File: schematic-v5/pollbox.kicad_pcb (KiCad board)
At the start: 2 copper layers, 50.8 x 74.9 mm, 24 parts, among them P1 CONN_01X15, P10 CONN_01X04, P2 CONN_02X03, P20 CONN_01X04, P3 CONN_01X15, P30 CONN_01X04, P40 CONN_01X04, P50 CONN_01X04, U1 NodeMCU_1.0, U2 ULN2803

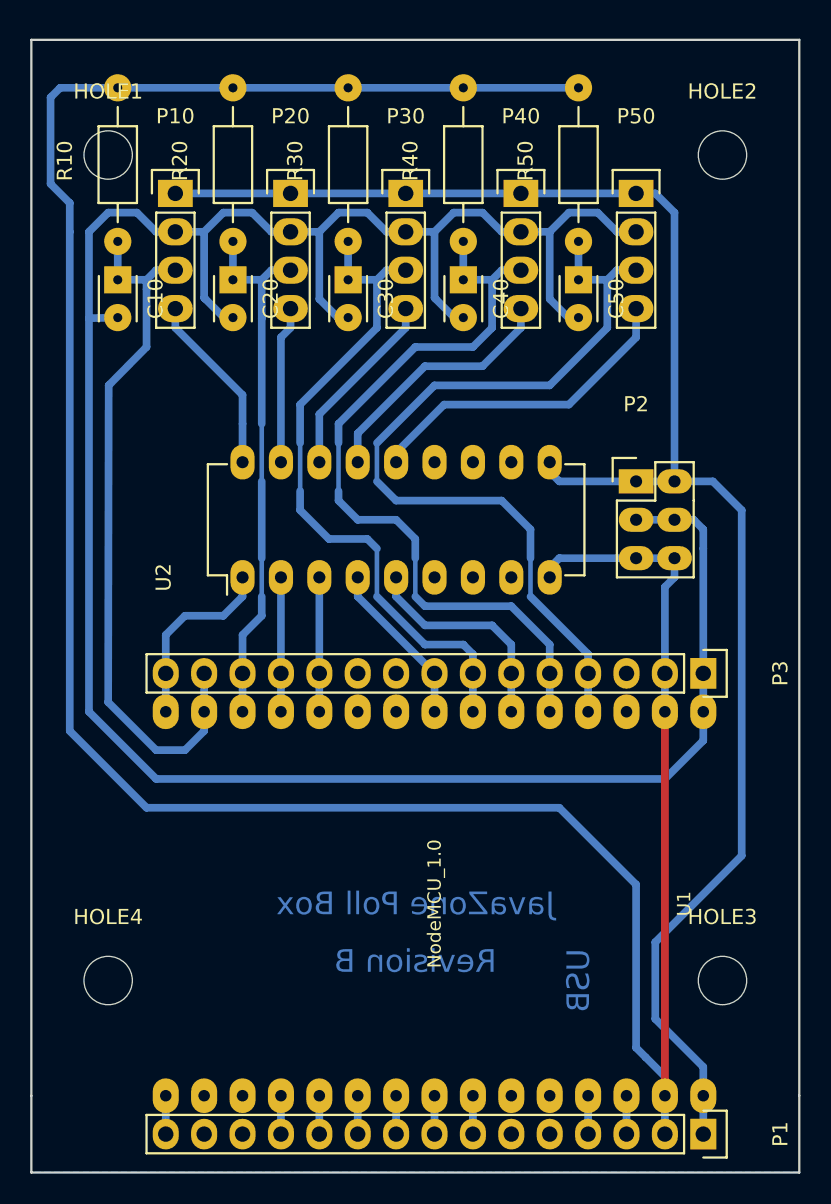
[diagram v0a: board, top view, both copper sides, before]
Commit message: reduce islands
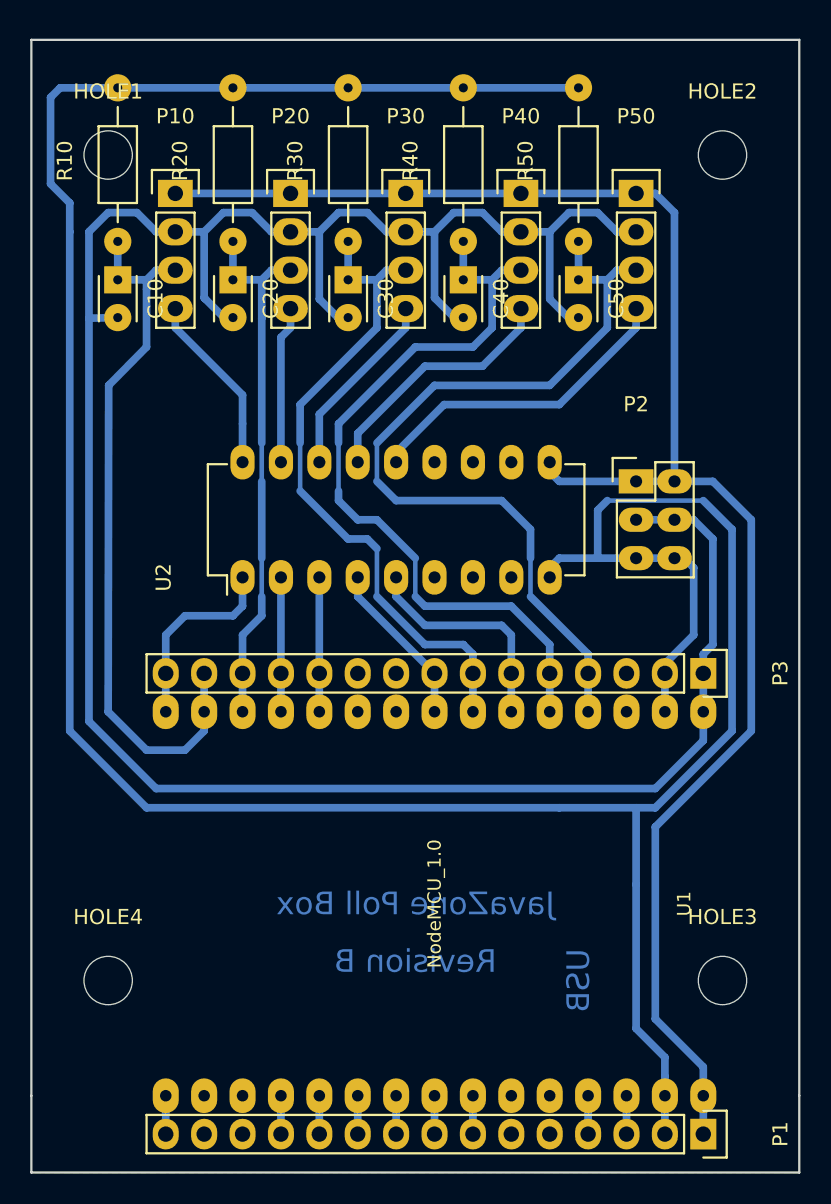
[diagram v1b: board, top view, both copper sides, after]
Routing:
- net GND: track 181.6 -> 195.5 mm
- net +3V3: track 168.6 -> 170.0 mm
- net /SWITCH_4: track 52.3 -> 51.5 mm
- net /SWITCH_3: track 45.4 -> 44.7 mm
- net +5V: track 111.3 -> 111.8 mm

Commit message: fix conflict with mounting holes
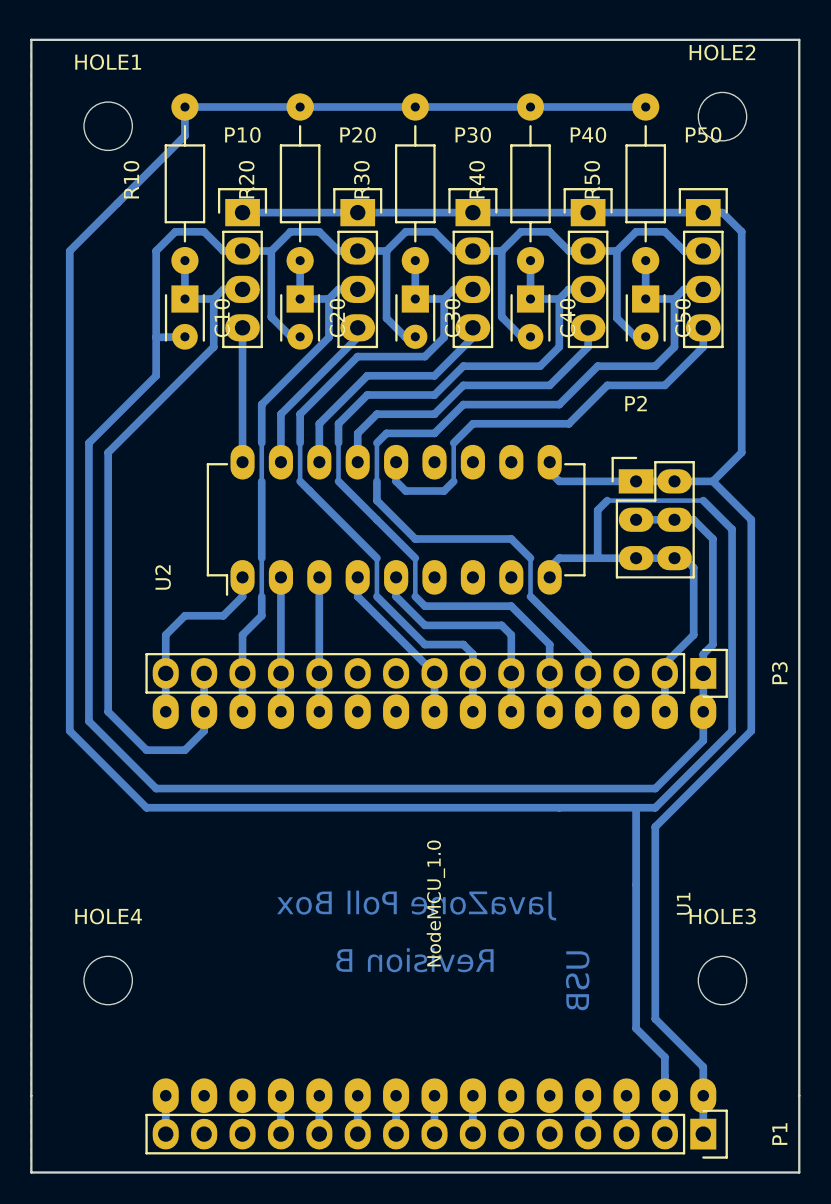
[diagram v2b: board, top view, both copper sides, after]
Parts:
- moved P20 4.62 mm to (99.1, 55.9)
- moved P30 4.62 mm to (106.7, 55.9)
- moved P50 4.62 mm to (121.9, 55.9)
- moved R30 4.62 mm to (102.9, 54.0)
- moved C30 4.62 mm to (102.9, 61.6)
- moved P10 4.62 mm to (91.4, 55.9)
- moved P40 4.62 mm to (114.3, 55.9)
- moved R10 4.62 mm to (87.6, 54.0)
- moved R20 4.62 mm to (95.2, 54.0)
- moved R40 4.62 mm to (110.5, 54.0)
- moved R50 4.62 mm to (118.1, 54.0)
- moved C10 4.62 mm to (87.6, 61.6)
- moved C20 4.62 mm to (95.2, 61.6)
- moved C40 4.62 mm to (110.5, 61.6)
- moved C50 4.62 mm to (118.1, 61.6)
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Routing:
- net /LED_5_OUT: track 21.2 -> 29.2 mm
- net /LED_4_OUT: track 17.5 -> 21.4 mm
- net /SWITCH_5: track 56.5 -> 60.0 mm
- net /LED_3_OUT: track 13.2 -> 16.3 mm
- net /SWITCH_4: track 51.5 -> 54.7 mm
- net /LED_1_OUT: track 12.0 -> 8.89 mm
- net GND: track 195.5 -> 192.8 mm
- net /SWITCH_3: track 44.7 -> 47.1 mm
- net /LED_1: track 48.6 -> 49.2 mm
- net +3V3: track 170.0 -> 170.6 mm
- net /SWITCH_2: track 35.7 -> 36.3 mm
- net /LED_2_OUT: track 10.4 -> 11.0 mm

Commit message: some more routes cleanup
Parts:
- moved P10 0.64 mm to (91.4, 55.2)
- moved P20 0.64 mm to (99.1, 55.2)
- moved P30 0.64 mm to (106.7, 55.2)
- moved P40 0.64 mm to (114.3, 55.2)
- moved P50 0.64 mm to (121.9, 55.2)
- moved C10 0.63 mm to (87.6, 61.0)
- moved C20 0.63 mm to (95.2, 61.0)
- moved C30 0.63 mm to (102.9, 61.0)
- moved C40 0.63 mm to (110.5, 61.0)
- moved C50 0.63 mm to (118.1, 61.0)
- moved HOLE1 0.63 mm to (82.5, 49.5)
- moved R10 0.63 mm to (87.6, 53.3)
- moved R20 0.63 mm to (95.2, 53.3)
- moved R30 0.63 mm to (102.9, 53.3)
- moved R40 0.63 mm to (110.5, 53.3)
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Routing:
- net /SWITCH_3: track 47.1 -> 49.3 mm
- net /LED_4: track 11.0 -> 13.2 mm
- net /LED_2_OUT: track 11.0 -> 12.3 mm
- net /LED_3_OUT: track 16.3 -> 17.6 mm
- net /LED_5: track 15.0 -> 14.1 mm
- net /LED_5_OUT: track 29.2 -> 29.9 mm
- net /SWITCH_2: track 36.3 -> 36.9 mm
- net +5V: track 111.4 -> 112.0 mm

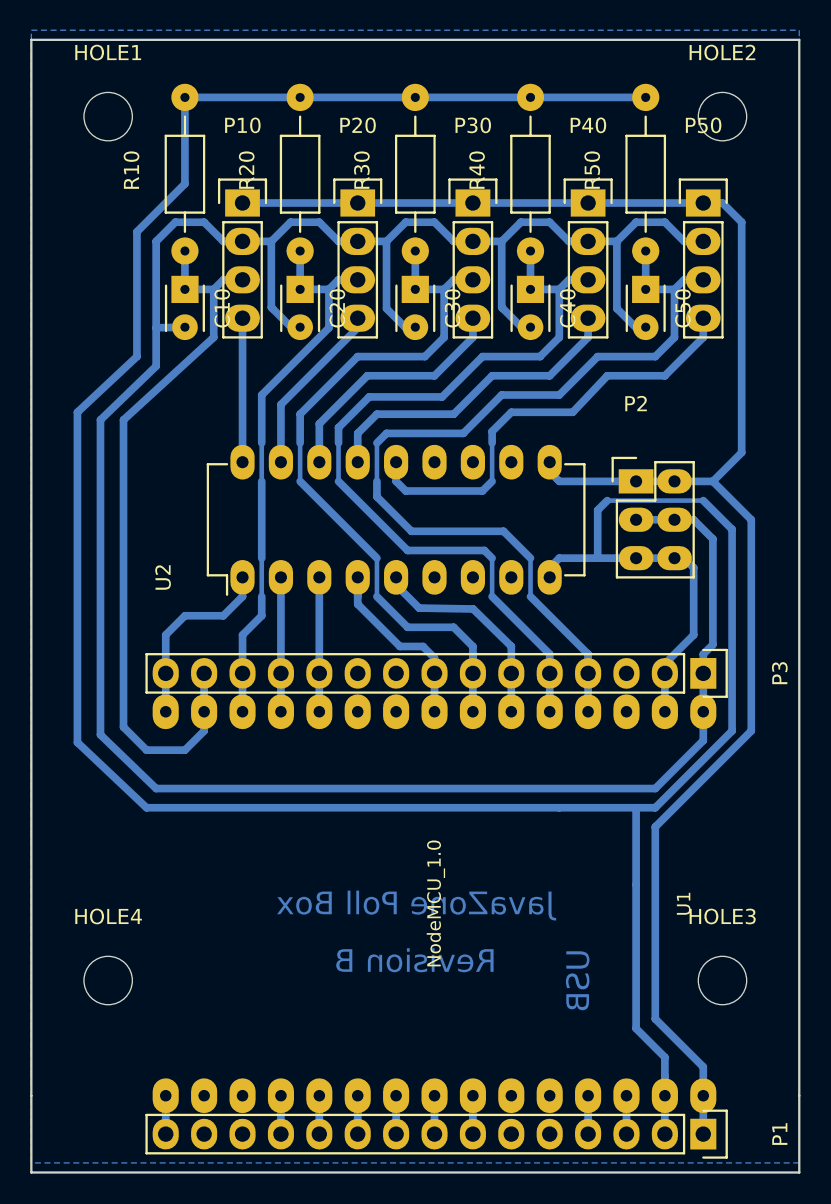
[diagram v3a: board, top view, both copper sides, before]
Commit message: o Shrinking the board size so we can fit 2x2 on a single board when etching. o Fixing too large NodeMCU footprint. Double checking, yay!
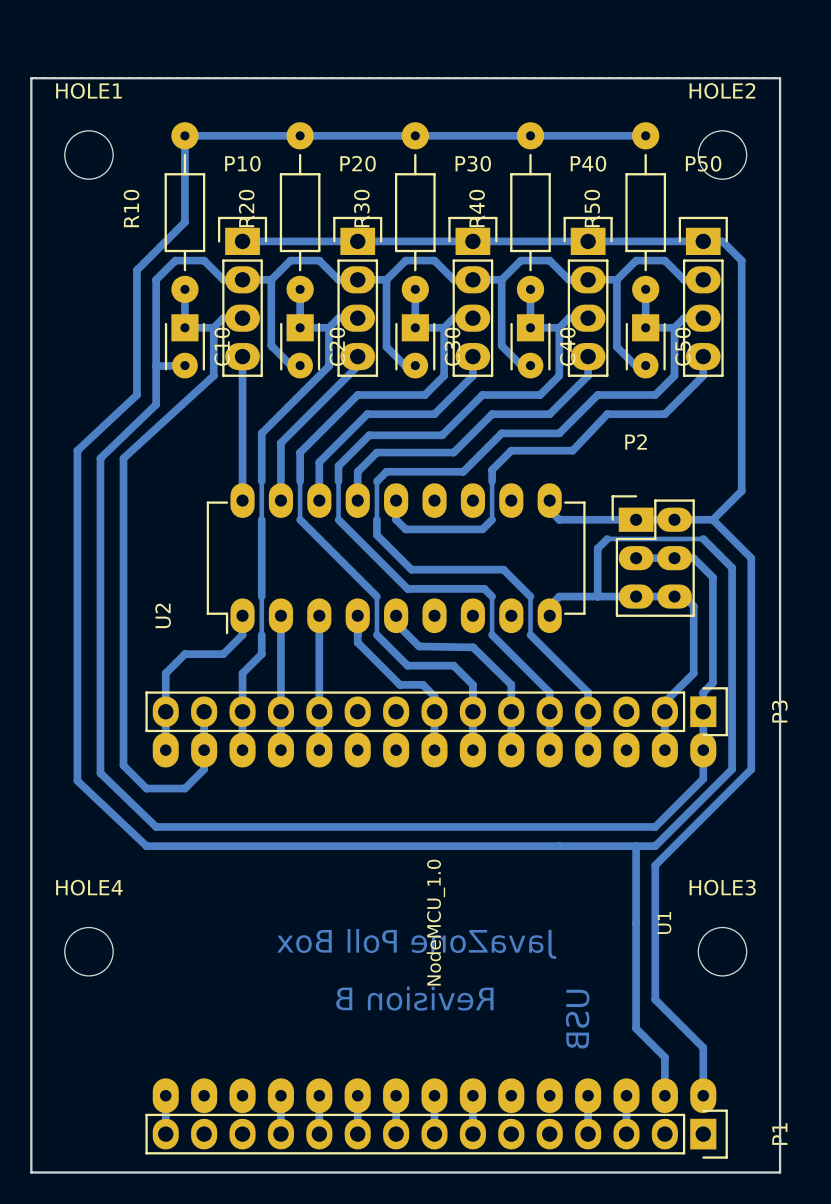
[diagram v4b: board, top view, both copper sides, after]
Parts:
- moved HOLE1 2.84 mm to (81.3, 52.1)
- moved P2 2.54 mm to (117.5, 76.2)
- moved P3 2.54 mm to (121.9, 88.9)
- moved C10 2.54 mm to (87.6, 63.5)
- moved C20 2.54 mm to (95.2, 63.5)
- moved C30 2.54 mm to (102.9, 63.5)
- moved C40 2.54 mm to (110.5, 63.5)
- moved C50 2.54 mm to (118.1, 63.5)
- moved HOLE2 2.54 mm to (123.2, 52.1)
- moved P10 2.54 mm to (91.4, 57.8)
- moved P20 2.54 mm to (99.1, 57.8)
- moved P30 2.54 mm to (106.7, 57.8)
- moved P40 2.54 mm to (114.3, 57.8)
- moved P50 2.54 mm to (121.9, 57.8)
- moved R10 2.54 mm to (87.6, 55.9)
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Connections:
- C10 pad 1: /LED_1 -> /SWITCH_1
- P1 pad 13: Net-(P1-Pad13) -> (no net)
- P1 pad 14: Net-(P1-Pad14) -> (no net)
- P1 pad 5: Net-(P1-Pad5) -> (no net)
- P1 pad 6: Net-(P1-Pad6) -> (no net)
- P10 pad 3: /LED_1 -> /SWITCH_1
- P3 pad 10: Net-(P3-Pad10) -> (no net)
- P3 pad 14: /LED_1 -> /SWITCH_1
- P3 pad 15: Net-(P3-Pad15) -> /LED_1
- P3 pad 3: Net-(P3-Pad3) -> (no net)
- P3 pad 9: Net-(P3-Pad9) -> (no net)
- R10 pad 1: /LED_1 -> /SWITCH_1
- U1 pad 13: Net-(U1-Pad13) -> (no net)
- U1 pad 14: Net-(U1-Pad14) -> (no net)
- U1 pad 16: Net-(P3-Pad15) -> /LED_1
- U1 pad 17: /LED_1 -> /SWITCH_1
- U1 pad 21: Net-(U1-Pad21) -> (no net)
- U1 pad 22: Net-(U1-Pad22) -> (no net)
- U1 pad 28: Net-(U1-Pad28) -> (no net)
- U1 pad 5: Net-(U1-Pad5) -> (no net)
- U1 pad 6: Net-(U1-Pad6) -> (no net)
- U2 pad 1: Net-(P3-Pad15) -> /LED_1
- U2 pad 11: Net-(U2-Pad11) -> (no net)
- U2 pad 12: Net-(U2-Pad12) -> (no net)
- U2 pad 13: Net-(U2-Pad13) -> (no net)
- U2 pad 6: Net-(U2-Pad6) -> (no net)
- U2 pad 7: Net-(U2-Pad7) -> (no net)
- U2 pad 8: Net-(U2-Pad8) -> (no net)
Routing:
- net /SWITCH_1: track 0.00 -> 49.8 mm
- net /LED_1: track 49.1 -> 11.8 mm
- net Net-(P3-Pad15): track 12.5 -> 0.00 mm
- net +5V: track 112.0 -> 106.9 mm
- net GND: track 193.1 -> 188.7 mm
- net /SWITCH_5: track 60.1 -> 59.5 mm
- net /SWITCH_4: track 54.4 -> 53.8 mm
- net /SWITCH_2: track 36.9 -> 36.3 mm
- net /LED_5: track 14.1 -> 13.5 mm
- net /LED_4: track 13.2 -> 12.5 mm
- net /LED_3: track 8.89 -> 8.26 mm
- net /LED_2: track 8.89 -> 8.26 mm
- net /SWITCH_3: track 49.3 -> 48.7 mm
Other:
- board size 50.8 x 74.9 mm -> 49.5 x 72.4 mm

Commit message: add missing wires
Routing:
- net GND: track 188.7 -> 191.2 mm
- net +5V: track 106.9 -> 109.4 mm
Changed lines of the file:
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@@
-(kicad_pcb (version 4) (host pcbnew 4.0.2+dfsg1-stable)
+(kicad_pcb (version 4) (host pcbnew 4.0.3-stable)
   (general
     (links 77)
-    (no_connects 2)
-    (area 77.394999 43.739999 127.075001 118.820001)
+    (no_connects 0)
+    (area 65.810001 40.48 132.801143 121.927333)
     (thickness 1.6)
     (drawings 9)
-    (tracks 279)
+    (tracks 281)
     (zones 0)
     (modules 24)
@@
   (segment (start 118.11 66) (end 117.435 66) (width 0.3048) (layer B.Cu) (net 1) (status 30))
   (segment (start 121.92 90.805) (end 121.92 90.805) (width 0.508) (layer B.Cu) (net 1) (status 30))
+  (segment (start 121.92 114.3) (end 121.92 116.84) (width 0.508) (layer B.Cu) (net 2))
   (segment (start 121.92 114.3) (end 121.92 111.125) (width 0.508) (layer B.Cu) (net 2))
   (segment (start 121.92 111.125) (end 118.745 107.95) (width 0.508) (layer B.Cu) (net 2))
@@
   (segment (start 106.68 57.785) (end 114.3 57.785) (width 0.508) (layer B.Cu) (net 2) (status 30))
   (segment (start 99.06 57.785) (end 106.68 57.785) (width 0.508) (layer B.Cu) (net 2) (status 10))
+  (segment (start 119.38 114.3) (end 119.38 116.84) (width 0.508) (layer B.Cu) (net 3))
   (segment (start 119.38 114.3) (end 119.38 111.76) (width 0.508) (layer B.Cu) (net 3))
   (segment (start 119.38 111.76) (end 117.475 109.855) (width 0.508) (layer B.Cu) (net 3))
@@
     (polygon
       (pts
-        (xy 127 119.38) (xy 77.47 119.38) (xy 77.47 46.99) (xy 127 46.99) (xy 127 119.38)
+        (xy 127 119.38) (xy 77.47 119.38) (xy 77.47 46.99) (xy 127 46.99)
       )
     )
